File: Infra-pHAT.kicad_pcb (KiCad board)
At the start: 2 copper layers, 65 x 30 mm, 25 parts, among them Q1 BC817, U1 CAT24C32WI-GT3

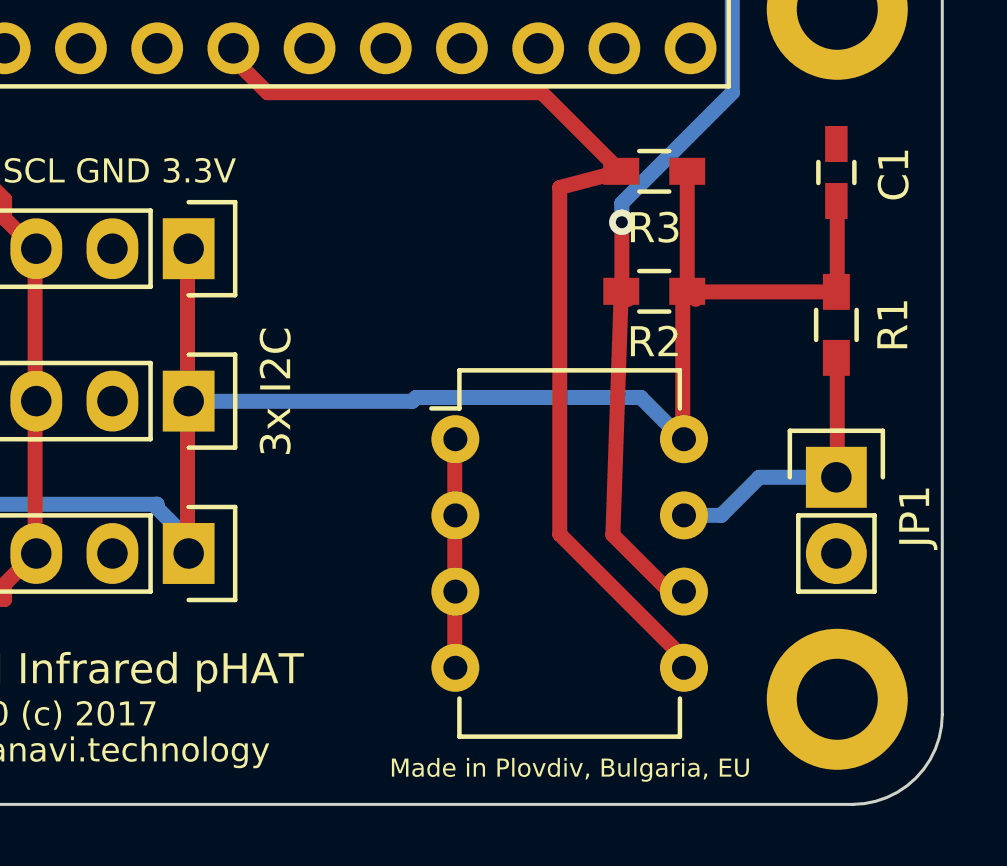
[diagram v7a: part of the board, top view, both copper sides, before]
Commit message: deleted the DIP8 footprint for CAT24C32WI-GT3
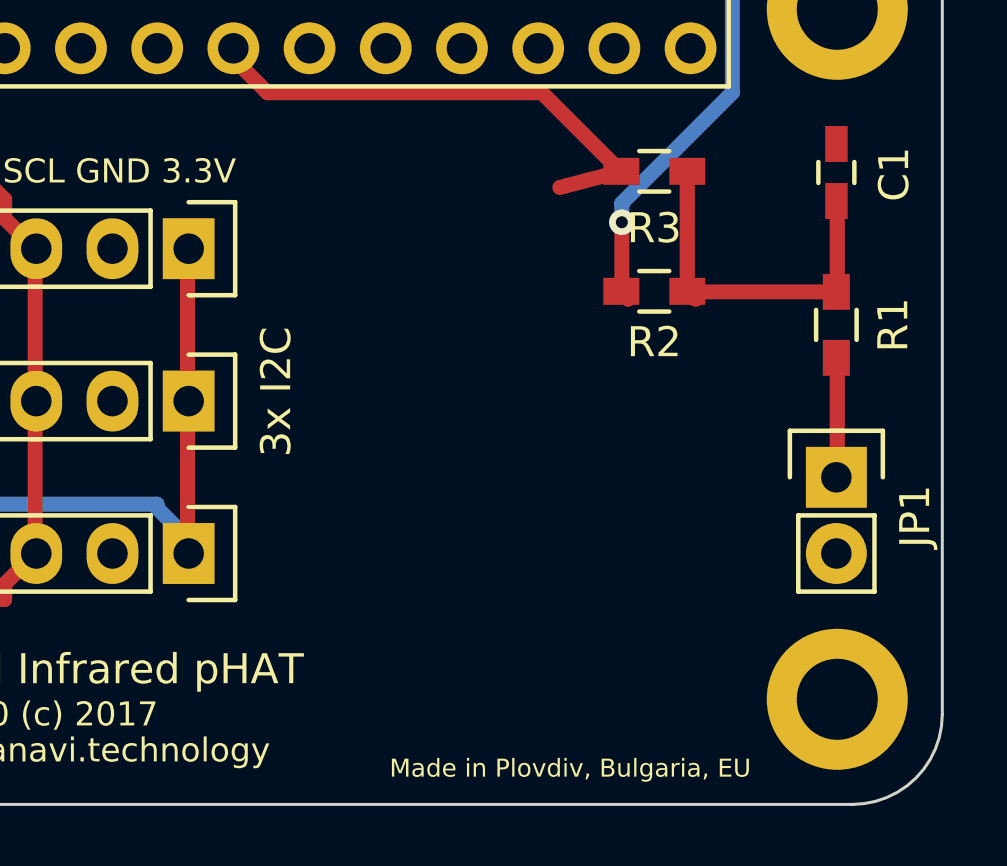
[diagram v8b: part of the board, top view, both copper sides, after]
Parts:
- removed U1: CAT24C32WI-GT3, Housings_DIP:DIP-8_W7.62mm
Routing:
- net +3V3: track 105.5 -> 83.4 mm
- net Net-(R3-Pad2): track 35.1 -> 17.2 mm
- net Net-(R2-Pad2): track 42.8 -> 31.4 mm
- net GND: track 8.40 -> 0.00 mm
- net Net-(JP1-Pad1): track 10.1 -> 4.33 mm
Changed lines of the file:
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@@
     (thickness 1.6)
     (drawings 31)
-    (tracks 239)
+    (tracks 209)
     (zones 0)
-    (modules 25)
+    (modules 24)
     (nets 36)
   )
@@
     )
   )
-  (module Housings_DIP:DIP-8_W7.62mm (layer F.Cu)
-    (at 197.27 92.83)
-    (descr "8-lead dip package, row spacing 7.62 mm (300 mils)")
-    (tags "dil dip 2.54 300")
-    (fp_text reference U1 (at 0 -5.22) (layer F.SilkS) hide
-      (effects (font (size 1 1) (thickness 0.15)))
-    )
-    (fp_text value CAT24C32WI-GT3 (at 0 -3.72) (layer F.Fab) hide
-      (effects (font (size 1 1) (thickness 0.15)))
-    )
-    (fp_line (start -1.05 -2.45) (end -1.05 10.1) (layer F.CrtYd) (width 0.05))
-    (fp_line (start 8.65 -2.45) (end 8.65 10.1) (layer F.CrtYd) (width 0.05))
-    (fp_line (start -1.05 -2.45) (end 8.65 -2.45) (layer F.CrtYd) (width 0.05))
-    (fp_line (start -1.05 10.1) (end 8.65 10.1) (layer F.CrtYd) (width 0.05))
-    (fp_line (start 0.135 -2.295) (end 0.135 -1.025) (layer F.SilkS) (width 0.15))
-    (fp_line (start 7.485 -2.295) (end 7.485 -1.025) (layer F.SilkS) (width 0.15))
-    (fp_line (start 7.485 9.915) (end 7.485 8.645) (layer F.SilkS) (width 0.15))
-    (fp_line (start 0.135 9.915) (end 0.135 8.645) (layer F.SilkS) (width 0.15))
-    (fp_line (start 0.135 -2.295) (end 7.485 -2.295) (layer F.SilkS) (width 0.15))
-    (fp_line (start 0.135 9.915) (end 7.485 9.915) (layer F.SilkS) (width 0.15))
-    (fp_line (start 0.135 -1.025) (end -0.8 -1.025) (layer F.SilkS) (width 0.15))
-    (pad 1 thru_hole oval (at 0 0) (size 1.6 1.6) (drill 0.8) (layers *.Cu *.Mask F.SilkS)
-      (net 2 GND))
-    (pad 2 thru_hole oval (at 0 2.54) (size 1.6 1.6) (drill 0.8) (layers *.Cu *.Mask F.SilkS)
-      (net 2 GND))
-    (pad 3 thru_hole oval (at 0 5.08) (size 1.6 1.6) (drill 0.8) (layers *.Cu *.Mask F.SilkS)
-      (net 2 GND))
-    (pad 4 thru_hole oval (at 0 7.62) (size 1.6 1.6) (drill 0.8) (layers *.Cu *.Mask F.SilkS)
-      (net 2 GND))
-    (pad 5 thru_hole oval (at 7.62 7.62) (size 1.6 1.6) (drill 0.8) (layers *.Cu *.Mask F.SilkS)
-      (net 9 "Net-(R3-Pad2)"))
-    (pad 6 thru_hole oval (at 7.62 5.08) (size 1.6 1.6) (drill 0.8) (layers *.Cu *.Mask F.SilkS)
-      (net 8 "Net-(R2-Pad2)"))
-    (pad 7 thru_hole oval (at 7.62 2.54) (size 1.6 1.6) (drill 0.8) (layers *.Cu *.Mask F.SilkS)
-      (net 6 "Net-(JP1-Pad1)"))
-    (pad 8 thru_hole oval (at 7.62 0) (size 1.6 1.6) (drill 0.8) (layers *.Cu *.Mask F.SilkS)
-      (net 1 +3V3))
-    (model Housings_DIP.3dshapes/DIP-8_W7.62mm.wrl
-      (at (xyz 0 0 0))
-      (scale (xyz 1 1 1))
-      (rotate (xyz 0 0 0))
-    )
-  )
   (module Pin_Headers:Pin_Header_Straight_1x04 (layer F.Cu)
     (at 167.1 86.5 90)
@@
   (gr_arc (start 151.5011 102.0036) (end 148.5011 102.0036) (angle -90) (layer Edge.Cuts) (width 0.1))
   (gr_circle (center 152.0011 101.5036) (end 152.0011 101.5036) (layer Edge.Cuts) (width 0.1))
-  (segment (start 204.89 92.83) (end 204.851 92.837) (width 0.5) (layer B.Cu) (net 1) (status 80000))
-  (segment (start 204.851 92.837) (end 203.454 91.44) (width 0.5) (layer B.Cu) (net 1) (status 80000))
-  (segment (start 203.454 91.44) (end 195.961 91.44) (width 0.5) (layer B.Cu) (net 1) (status 80000))
-  (segment (start 195.961 91.44) (end 195.834 91.567) (width 0.5) (layer B.Cu) (net 1) (status 80000))
-  (segment (start 195.834 91.567) (end 188.341 91.567) (width 0.5) (layer B.Cu) (net 1) (status 80000))
   (segment (start 188.341 91.567) (end 188.38 91.56) (width 0.5) (layer B.Cu) (net 1) (status 80000))
   (segment (start 205 87.9) (end 204.978 87.884) (width 0.5) (layer F.Cu) (net 1) (status 80000))
   (segment (start 204.978 87.884) (end 204.851 88.011) (width 0.5) (layer F.Cu) (net 1) (status 80000))
-  (segment (start 204.851 88.011) (end 204.851 92.837) (width 0.5) (layer F.Cu) (net 1) (status 80000))
-  (segment (start 204.851 92.837) (end 204.89 92.83) (width 0.5) (layer F.Cu) (net 1) (status 80000))
   (segment (start 205 83.9) (end 205 87.9) (width 0.5) (layer F.Cu) (net 1))
   (segment (start 209.97 87.92) (end 205.02 87.92) (width 0.5) (layer F.Cu) (net 1))
@@
   (segment (start 205 87.9) (end 205.03 87.92) (width 0.5) (layer F.Cu) (net 1) (status 80030))
   (segment (start 205.03 87.92) (end 205.28 88.17) (width 0.5) (layer F.Cu) (net 1) (status 80030))
-  (segment (start 205 92.75) (end 204.89 92.83) (width 0.5) (layer F.Cu) (net 1) (status 80000))
-  (segment (start 197.25 92.75) (end 197.27 92.83) (width 0.5) (layer B.Cu) (net 2) (status 80000))
-  (segment (start 197.27 95.37) (end 197.25 95.25) (width 0.5) (layer F.Cu) (net 2) (status 80000))
-  (segment (start 197.25 95.25) (end 197.25 98) (width 0.5) (layer F.Cu) (net 2) (status 80000))
-  (segment (start 197.25 98) (end 197.27 97.91) (width 0.5) (layer F.Cu) (net 2) (status 80000))
-  (segment (start 197.27 92.83) (end 197.25 92.75) (width 0.5) (layer F.Cu) (net 2) (status 80000))
-  (segment (start 197.25 92.75) (end 197.25 95.25) (width 0.5) (layer F.Cu) (net 2) (status 80000))
-  (segment (start 197.25 95.25) (end 197.27 95.37) (width 0.5) (layer F.Cu) (net 2) (status 80000))
-  (segment (start 197.27 97.91) (end 197.25 98) (width 0.5) (layer F.Cu) (net 2) (status 80000))
-  (segment (start 197.25 98) (end 197.25 100.5) (width 0.5) (layer F.Cu) (net 2) (status 80000))
-  (segment (start 197.25 100.5) (end 197.27 100.45) (width 0.5) (layer F.Cu) (net 2) (status 80000))
   (segment (start 169.31 96.64) (end 169.291 96.647) (width 0.5) (layer F.Cu) (net 3) (status 80000))
   (segment (start 169.291 96.647) (end 169.291 102.235) (width 0.5) (layer F.Cu) (net 3) (status 80000))
@@
   (segment (start 152.781 90.932) (end 152.781 92.837) (width 0.5) (layer B.Cu) (net 5) (status 80000))
   (segment (start 152.781 92.837) (end 152.82 92.83) (width 0.5) (layer B.Cu) (net 5) (status 80000))
-  (segment (start 204.89 95.37) (end 206.13 95.37) (width 0.5) (layer B.Cu) (net 6))
-  (segment (start 207.4 94.1) (end 209.97 94.1) (width 0.5) (layer B.Cu) (net 6))
-  (segment (start 206.13 95.37) (end 207.4 94.1) (width 0.5) (layer B.Cu) (net 6))
   (segment (start 209.97 94.1) (end 210 94) (width 0.5) (layer F.Cu) (net 6) (status 80000))
   (segment (start 210 94) (end 210 90) (width 0.5) (layer F.Cu) (net 6) (status 80000))
   (segment (start 210 90) (end 209.97 90.12) (width 0.5) (layer F.Cu) (net 6) (status 80000))
-  (segment (start 204.89 95.37) (end 205 95.25) (width 0.5) (layer B.Cu) (net 6) (status 80000))
   (segment (start 210 94) (end 209.97 94.1) (width 0.5) (layer B.Cu) (net 6) (status 80000))
   (segment (start 160.65 85.59924) (end 160.655 85.598) (width 0.5) (layer F.Cu) (net 7) (status 80000))
@@
   (segment (start 202.819 85.598) (end 202.819 87.884) (width 0.5) (layer F.Cu) (net 8) (status 80000))
   (segment (start 202.819 87.884) (end 202.8 87.9) (width 0.5) (layer F.Cu) (net 8) (status 80000))
-  (segment (start 204.89 97.91) (end 204.41 97.91) (width 0.5) (layer F.Cu) (net 8))
-  (segment (start 204.41 97.91) (end 202.52 96.02) (width 0.5) (layer F.Cu) (net 8))
-  (segment (start 202.52 96.02) (end 202.8 87.9) (width 0.5) (layer F.Cu) (net 8) (status 20))
   (segment (start 202.8 87.9) (end 203.03 88.17) (width 0.5) (layer F.Cu) (net 8) (status 80030))
-  (segment (start 205 98) (end 204.89 97.91) (width 0.5) (layer F.Cu) (net 8) (status 80000))
   (segment (start 202.8 83.9) (end 202.819 83.947) (width 0.5) (layer F.Cu) (net 9) (status 80000))
   (segment (start 202.819 83.947) (end 200.152 81.28) (width 0.5) (layer F.Cu) (net 9) (status 80000))
@@
   (segment (start 189.865 80.137) (end 189.865 79.756) (width 0.5) (layer F.Cu) (net 9) (status 80000))
   (segment (start 189.865 79.756) (end 189.87 79.8) (width 0.5) (layer F.Cu) (net 9) (status 80000))
-  (segment (start 204.89 100.45) (end 204.89 100.14) (width 0.5) (layer F.Cu) (net 9))
-  (segment (start 204.89 100.14) (end 200.75 96) (width 0.5) (layer F.Cu) (net 9))
   (segment (start 200.75 84.44) (end 202.8 83.9) (width 0.5) (layer F.Cu) (net 9) (status 20))
-  (segment (start 200.75 96) (end 200.75 84.44) (width 0.5) (layer F.Cu) (net 9))
   (segment (start 202.8 83.9) (end 202.78 83.98) (width 0.5) (layer F.Cu) (net 9) (status 80030))
-  (segment (start 205 100.5) (end 204.89 100.45) (width 0.5) (layer F.Cu) (net 9) (status 80000))
   (segment (start 180.76 86.48) (end 180.721 86.487) (width 0.5) (layer F.Cu) (net 10) (status 80000))
   (segment (start 180.721 86.487) (end 180.721 91.567) (width 0.5) (layer F.Cu) (net 10) (status 80000))
